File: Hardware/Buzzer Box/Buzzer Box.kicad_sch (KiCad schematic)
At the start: 39 parts, among them IC1 4691, IC10 4691, IC11 4691, IC12 4691, IC2 4691, IC3 4691, IC4 4691, IC5 4691, IC6 4691, IC7 4691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

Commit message: Updated the PCB
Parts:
- removed J15: IO42, Connector_Wire:SolderWirePad_1x01_SMD_1x2mm, symbol Connector:Conn_01x01_Pin
- removed J16: IO41, Connector_Wire:SolderWirePad_1x01_SMD_1x2mm, symbol Connector:Conn_01x01_Pin
- added C3, C4, C6, C7: 100n, Capacitor_SMD:C_0603_1608Metric_Pad1.08x0.95mm_HandSolder, symbol Device:C
- added H1, H2, H3, H4, H5: MountingHole_Pad, MountingHole:MountingHole_3.2mm_M3_ISO14580_Pad_TopBottom, symbol Mechanical:MountingHole_Pad
- added J2: UART, Connector_JST:JST_XH_B4B-XH-A_1x04_P2.50mm_Vertical, symbol Connector:Conn_01x04_Pin
- added J3: JTAG, Connector_JST:JST_XH_B4B-XH-A_1x04_P2.50mm_Vertical, symbol Connector:Conn_01x04_Pin
- C1: footprint Capacitor_SMD:C_0603_1608Metric_Pad1.08x0.95mm_HandSolder -> Capacitor_SMD:C_0603_1608Metric
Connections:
- net +3.3V: now also C3.2, C4.2, C6.2, C7.2
- net +5V: now also J2.4 (Pin_4)
- net GND: now also C3.1, C4.1, C6.1, C7.1, H1.1, H2.1, H3.1, H4.1, H5.1, J2.1 (Pin_1)
- net at J1.2 (Pin_2), U10.32 (IO39): now also J3.4 (Pin_4)
- net at U10.34 (IO41): now also J3.2 (Pin_2)
- net at J12.2 (Pin_2), U10.33 (IO40): now also J3.3 (Pin_3)
- net at U10.35 (IO42): now also J3.1 (Pin_1)
- net at U10.36 (RXD0): now also J2.3 (Pin_3)
- net at U10.37 (TXD0): now also J2.2 (Pin_2)
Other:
- moved on the sheet: IC1, IC10, IC11, IC12, IC2, IC3, IC4, IC5, IC6, IC7, IC8, IC9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

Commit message: made chages to the PCB
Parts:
- J1: value GPIO 2 + GND -> GPIO 39; footprint Connector_JST:JST_XH_B2B-XH-AM_1x02_P2.50mm_Vertical -> Connector_JST:JST_XH_B2B-XH-A_1x02_P2.50mm_Vertical
- J12: value GPIO 2 + GND -> GPIO 40; footprint Connector_JST:JST_XH_B2B-XH-AM_1x02_P2.50mm_Vertical -> Connector_JST:JST_XH_B2B-XH-A_1x02_P2.50mm_Vertical
- J6: value GPIO 2 + GND -> GPIO 38; footprint Connector_JST:JST_XH_B2B-XH-AM_1x02_P2.50mm_Vertical -> Connector_JST:JST_XH_B2B-XH-A_1x02_P2.50mm_Vertical
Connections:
- net +3.3V: now also J1.1 (Pin_1), J12.1 (Pin_1), J6.1 (Pin_1)
- net GND: no longer J1.1 (Pin_1), J12.1 (Pin_1), J6.1 (Pin_1)
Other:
- company: (none) -> EinfachTechnik
- title: (none) -> BuzzerPCB
- moved on the sheet: R16

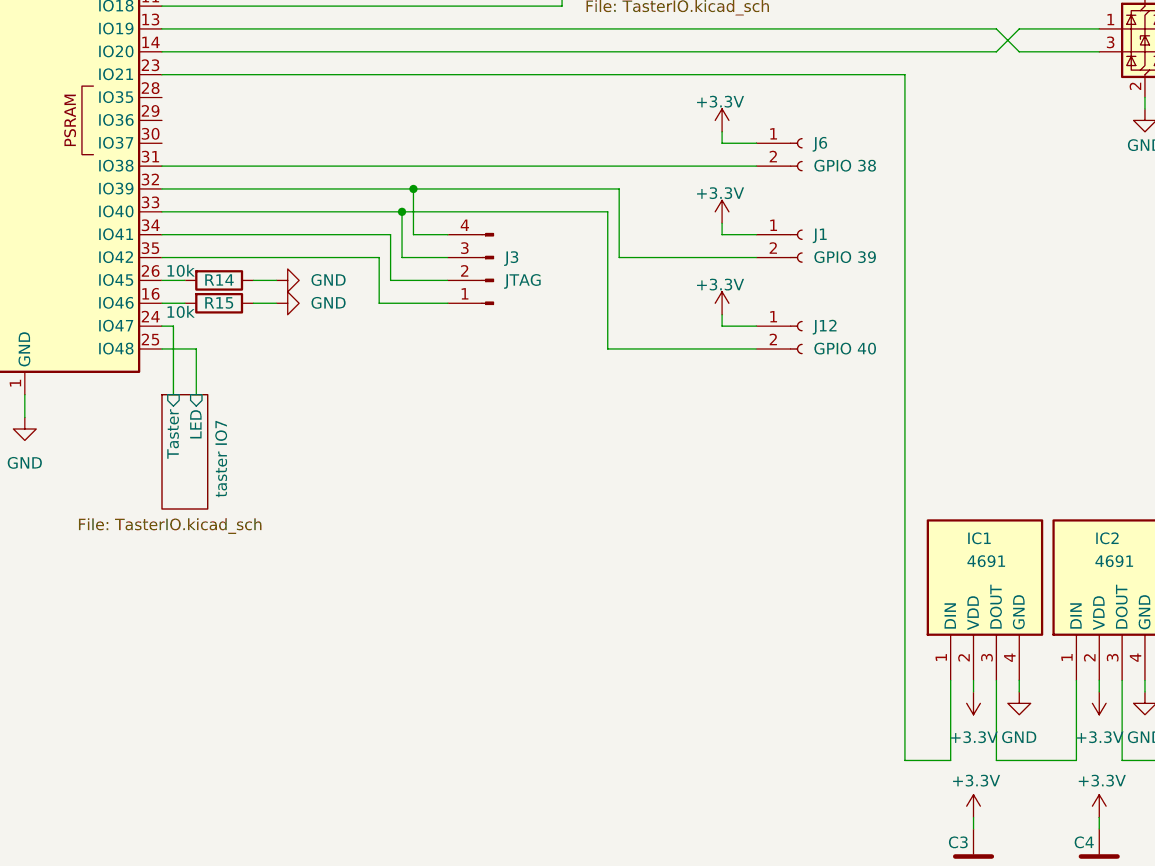
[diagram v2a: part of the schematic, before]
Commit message: added debouncing caps
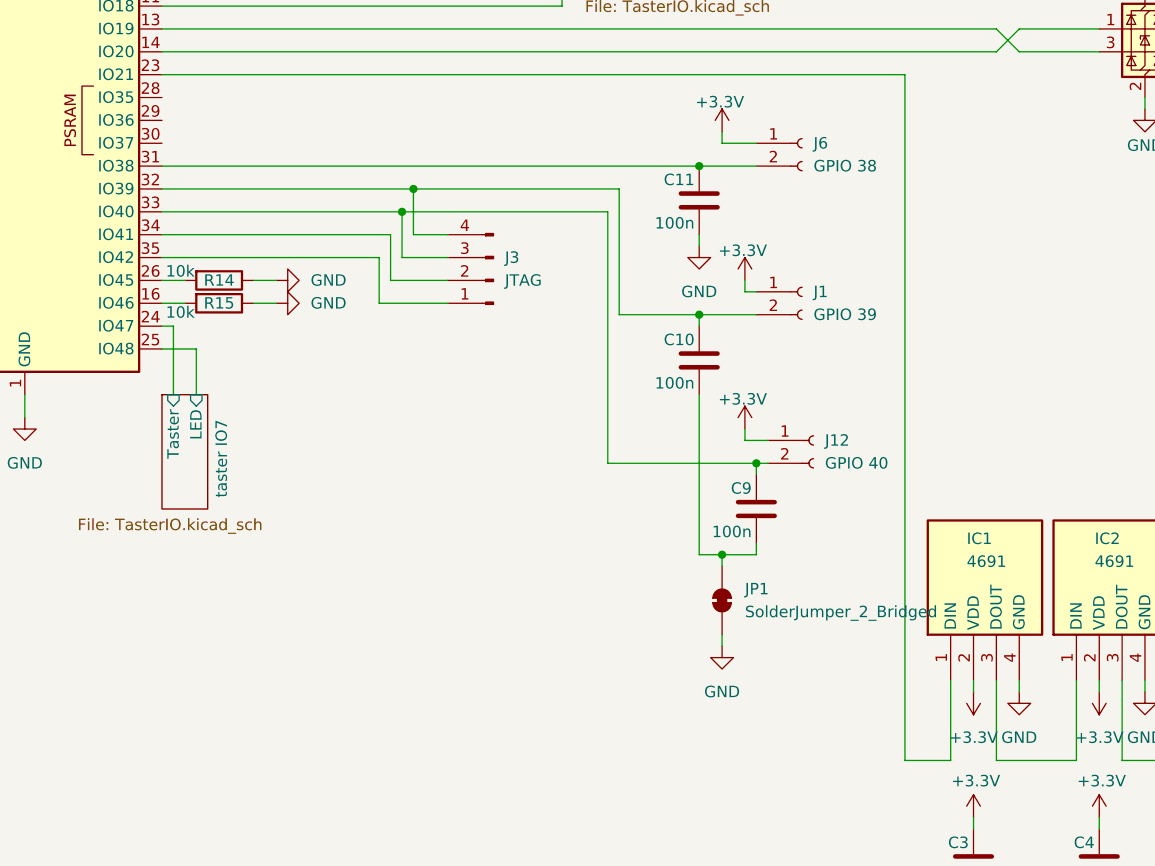
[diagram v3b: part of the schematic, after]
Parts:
- added C10, C11, C9: 100n, Capacitor_SMD:C_0603_1608Metric, symbol Device:C
- added JP1: SolderJumper_2_Bridged, Jumper:SolderJumper-2_P1.3mm_Bridged_Pad1.0x1.5mm, symbol Jumper:SolderJumper_2_Bridged
- C3, C4, C6, C7: footprint Capacitor_SMD:C_0603_1608Metric_Pad1.08x0.95mm_HandSolder -> Capacitor_SMD:C_0603_1608Metric
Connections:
- net GND: now also C11.1, JP1.1 (A)
- net at J1.2 (Pin_2), J3.4 (Pin_4), U10.32 (IO39): now also C10.2
- net at J12.2 (Pin_2), J3.3 (Pin_3), U10.33 (IO40): now also C9.2
- net at J6.2 (Pin_2), U10.31 (IO38): now also C11.2
- new net: C10.1, C9.1, JP1.2 (B)
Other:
- moved on the sheet: J1, J12

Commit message: final version
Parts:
- removed C10, C11, C9: 100n, Capacitor_SMD:C_0603_1608Metric, symbol Device:C
- removed J1: GPIO 39, Connector_JST:JST_XH_B2B-XH-A_1x02_P2.50mm_Vertical, symbol Connector:Conn_01x02_Socket
- removed J12: GPIO 40, Connector_JST:JST_XH_B2B-XH-A_1x02_P2.50mm_Vertical, symbol Connector:Conn_01x02_Socket
- removed J2: UART, Connector_JST:JST_XH_B4B-XH-A_1x04_P2.50mm_Vertical, symbol Connector:Conn_01x04_Pin
- removed J3: JTAG, Connector_JST:JST_XH_B4B-XH-A_1x04_P2.50mm_Vertical, symbol Connector:Conn_01x04_Pin
- removed J6: GPIO 38, Connector_JST:JST_XH_B2B-XH-A_1x02_P2.50mm_Vertical, symbol Connector:Conn_01x02_Socket
- removed JP1: SolderJumper_2_Bridged, Jumper:SolderJumper-2_P1.3mm_Bridged_Pad1.0x1.5mm, symbol Jumper:SolderJumper_2_Bridged
- added J2: JTAG, kiCadLibs:490107670612, symbol Connector:Conn_01x06_Pin
- added J6: UART, kiCadLibs:490107670612, symbol Connector:Conn_01x06_Pin
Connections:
- net +3.3V: now also J2.1 (Pin_1), J6.1 (Pin_1)
- net GND: now also J2.6 (Pin_6), J6.6 (Pin_6)
- net RST: now reaches C1.2, R11.1, S1.1 (COM_1), U10.3 (EN)
- net RST: now also J6.2 (Pin_2)
- net OI0: now reaches R16.2, R2.1, U10.27 (IO0)
- net OI0: now also J6.5 (Pin_5)
- net MTCK: now reaches U10.32 (IO39)
- net MTCK: now also J2.4 (Pin_4)
- net MTMS: now reaches U10.35 (IO42)
- net MTMS: now also J2.2 (Pin_2)
- net MTDI: now reaches U10.34 (IO41)
- net MTDI: now also J2.3 (Pin_3)
- net MTDO: now reaches U10.33 (IO40)
- net MTDO: now also J2.5 (Pin_5)
- net TX0: now reaches U10.37 (TXD0)
- net TX0: now also J6.3 (Pin_3)
- net RX0: now reaches U10.36 (RXD0)
- net RX0: now also J6.4 (Pin_4)
- net IOin/out: now reaches U10.31 (IO38)
- net IOin2/out: now reaches U10.38 (IO2)
- net IOin1/out: now reaches U10.39 (IO1)
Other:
- added sheet IOin (IOin.kicad_sch)
- added sheet IOin1 (IOin.kicad_sch)
- added sheet IOin2 (IOin.kicad_sch)
- moved on the sheet: C1, R11, R16, R2, S1, S2

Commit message: some changes
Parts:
- C2, C8: footprint Capacitor_SMD:C_0603_1608Metric_Pad1.08x0.95mm_HandSolder -> Capacitor_SMD:C_0603_1608Metric
- IC1, IC10, IC11, IC12, IC2, IC3, IC4, IC5, IC6, IC7, IC8, IC9: footprint 4691 -> Felix_LED:4691
- J2, J6: footprint kiCadLibs:490107670612 -> Felix_ProgHeader:490107670612
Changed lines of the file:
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@@
 			)
 		)
-		(property "Footprint" "4691"
+		(property "Footprint" "Felix_LED:4691"
 			(at 473.38 168.91 0)
 			(effects
@@
 			)
 		)
-		(property "Footprint" "4691"
+		(property "Footprint" "Felix_LED:4691"
 			(at 347.65 168.91 0)
 			(effects
@@
 			)
 		)
-		(property "Footprint" "4691"
+		(property "Footprint" "Felix_LED:4691"
 			(at 445.44 168.91 0)
 			(effects
@@
 			)
 		)
-		(property "Footprint" "Capacitor_SMD:C_0603_1608Metric_Pad1.08x0.95mm_HandSolder"
+		(property "Footprint" "Capacitor_SMD:C_0603_1608Metric"
 			(at 142.5448 80.01 0)
 			(effects
@@
 			)
 		)
-		(property "Footprint" "4691"
+		(property "Footprint" "Felix_LED:4691"
 			(at 459.41 168.91 0)
 			(effects
@@
 			)
 		)
-		(property "Footprint" "4691"
+		(property "Footprint" "Felix_LED:4691"
 			(at 361.62 168.91 0)
 			(effects
@@
 			)
 		)
-		(property "Footprint" "4691"
+		(property "Footprint" "Felix_LED:4691"
 			(at 417.5 168.91 0)
 			(effects
@@
 			)
 		)
-		(property "Footprint" "kiCadLibs:490107670612"
+		(property "Footprint" "Felix_ProgHeader:490107670612"
 			(at 95.25 27.94 0)
 			(effects
@@
 			)
 		)
-		(property "Footprint" "4691"
+		(property "Footprint" "Felix_LED:4691"
 			(at 389.56 168.91 0)
 			(effects
@@
 			)
 		)
-		(property "Footprint" "4691"
+		(property "Footprint" "Felix_LED:4691"
 			(at 431.47 168.91 0)
 			(effects
@@
 			)
 		)
-		(property "Footprint" "4691"
+		(property "Footprint" "Felix_LED:4691"
 			(at 487.35 168.91 0)
 			(effects
@@
 			)
 		)
-		(property "Footprint" "4691"
+		(property "Footprint" "Felix_LED:4691"
 			(at 375.59 168.91 0)
 			(effects
@@
 			)
 		)
-		(property "Footprint" "Capacitor_SMD:C_0603_1608Metric_Pad1.08x0.95mm_HandSolder"
+		(property "Footprint" "Capacitor_SMD:C_0603_1608Metric"
 			(at 152.7048 80.01 0)
 			(effects
@@
 			)
 		)
-		(property "Footprint" "4691"
+		(property "Footprint" "Felix_LED:4691"
 			(at 333.68 168.91 0)
 			(effects
@@
 			)
 		)
-		(property "Footprint" "4691"
+		(property "Footprint" "Felix_LED:4691"
 			(at 403.53 168.91 0)
 			(effects
@@
 			)
 		)
-		(property "Footprint" "kiCadLibs:490107670612"
+		(property "Footprint" "Felix_ProgHeader:490107670612"
 			(at 95.25 55.88 0)
 			(effects

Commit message: Upgrade zu .net9
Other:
- note added: "680R von fb nach GND"
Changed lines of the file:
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@@
+		)
+	)
+	(text "680R von fb nach GND"
+		(exclude_from_sim no)
+		(at 245.618 39.116 0)
+		(effects
+			(font
+				(size 1.27 1.27)
+			)
 		)
 	)
